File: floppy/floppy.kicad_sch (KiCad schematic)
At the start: 4 parts, among them J1 driveint, J2 perslota, J3 perslotb

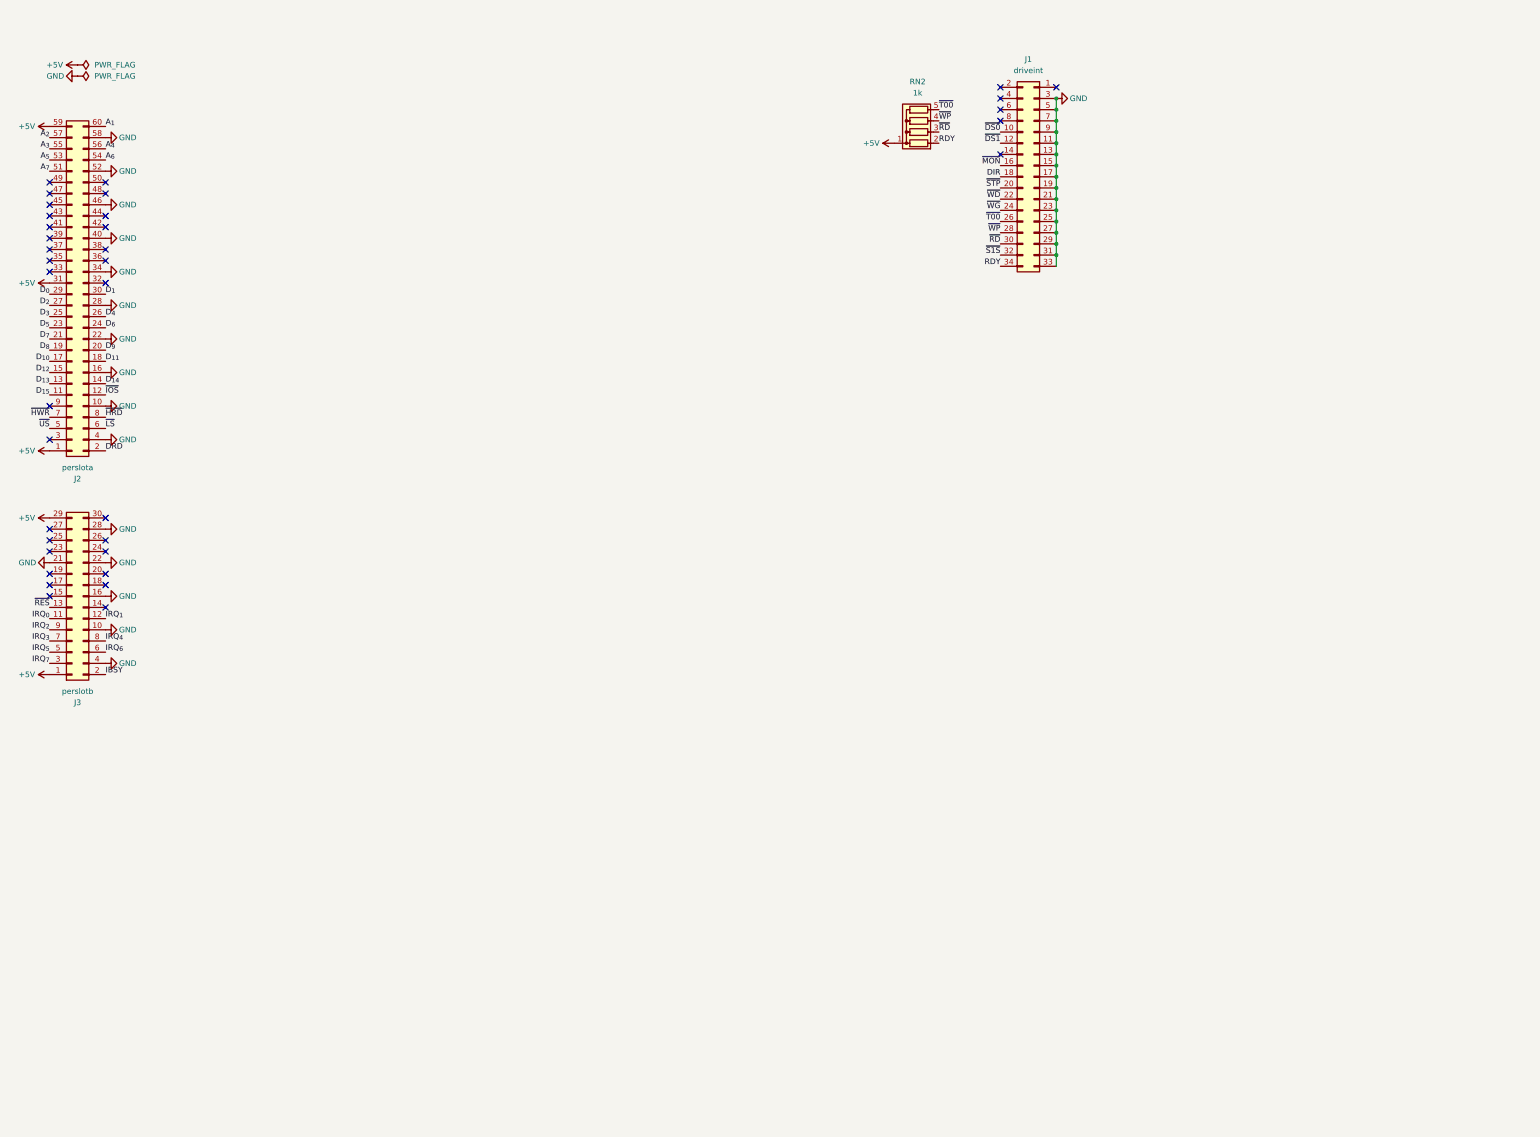
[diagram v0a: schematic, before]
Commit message: [floppy] added the 3.5" HD (custom) floppy controller peripheral
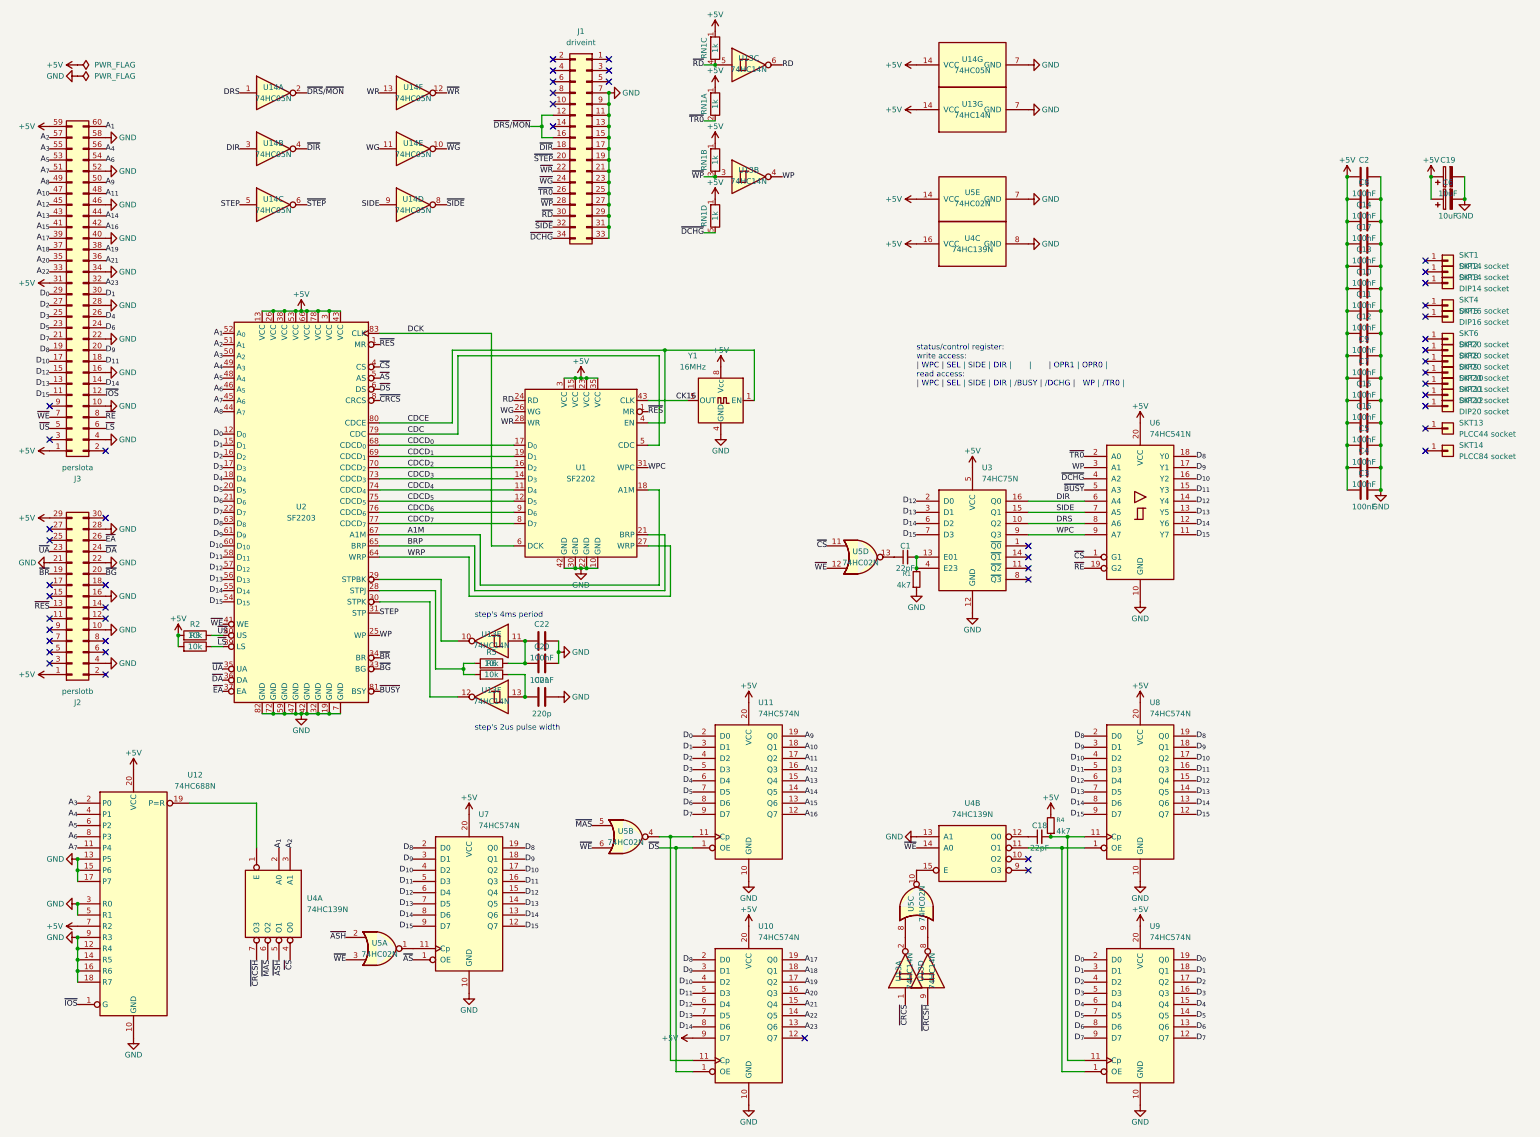
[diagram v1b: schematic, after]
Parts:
- removed RN2: 1k, Resistor_THT:R_Array_SIP5, symbol Device:R_Network04
- added C1, C18: 22pF, Capacitor_THT:C_Disc_D3.0mm_W1.6mm_P2.54mm, symbol Device:C_Small
- added C10, C11, C12, C13, C14, C17, C2, C20, C22, C7, C8, C9: 100nF, Capacitor_THT:C_Disc_D3.0mm_W1.6mm_P2.54mm, symbol Device:C
- added C15, C16, C3, C4, C5: 100nF, Capacitor_THT:C_Disc_D3.0mm_W1.6mm_P7.62mm, symbol Device:C
- added C19, C6: 10uF, Capacitor_THT:CP_Radial_D5.0mm_P2.00mm, symbol Device:C_Polarized
- added C21: 220p, Capacitor_THT:C_Disc_D3.0mm_W1.6mm_P2.54mm, symbol Device:C
- added R1, R4: 4k7, Resistor_THT:R_Axial_DIN0207_L6.3mm_D2.5mm_P2.54mm_Vertical, symbol Device:R_Small
- added R2, R3, R5, R6: 10k, Resistor_THT:R_Axial_DIN0207_L6.3mm_D2.5mm_P2.54mm_Vertical, symbol Device:R
- added RN1: 1k, Resistor_THT:R_Array_SIP5, symbol Device:R_Network04_Split
- added SKT1, SKT2, SKT3: DIP14 socket, symbol Connector_Generic:Conn_01x01
- added SKT10, SKT11, SKT12, SKT6, SKT7, SKT8, SKT9: DIP20 socket, symbol Connector_Generic:Conn_01x01
- added SKT13: PLCC44 socket, symbol Connector_Generic:Conn_01x01
- added SKT14: PLCC84 socket, symbol Connector_Generic:Conn_01x01
- added SKT4, SKT5: DIP16 socket, symbol Connector_Generic:Conn_01x01
- added U1: SF2202, Package_LCC:PLCC-44_THT-Socket, symbol SFxxxx:SF2202
- added U10, U11, U7, U8, U9: 74HC574N, Package_DIP:DIP-20_W7.62mm, symbol 74xx:74LS574
- added U12: 74HC688N, Package_DIP:DIP-20_W7.62mm, symbol 74xx:74HC688
- added U13: 74HC14N, Package_DIP:DIP-14_W7.62mm, symbol 74xx:74HC14
- added U14: 74HC05N, Package_DIP:DIP-14_W7.62mm, symbol 74xx:74LS05
- added U2: SF2203, Package_LCC:PLCC-84_THT-Socket, symbol SFxxxx:SF2203
- added U3: 74HC75N, Package_DIP:DIP-16_W7.62mm, symbol 74xx:74LS75
- added U4: 74HC139N, Package_DIP:DIP-16_W7.62mm, symbol 74xx:74LS139
- added U5: 74HC02N, Package_DIP:DIP-14_W7.62mm, symbol 74xx:74HC02
- added U6: 74HC541N, Package_DIP:DIP-20_W7.62mm, symbol 74xx:74LS541
- added Y1: 16MHz, Oscillator:Oscillator_DIP-8, symbol Oscillator:CXO_DIP8
- J1: footprint (none) -> Connector_IDC:IDC-Header_2x17_P2.54mm_Horizontal
- J2: renamed from J3; footprint Connector_IDC:IDC-Header_2x15_P2.54mm_Horizontal -> Connector_PCBEdge:edge_connector_15p_2.54mm; now left out of the parts list
- J3: renamed from J2; footprint Connector_IDC:IDC-Header_2x30_P2.54mm_Horizontal -> Connector_PCBEdge:edge_connector_30p_2.54mm; now left out of the parts list
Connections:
- net ~{MON} is gone; now on net ~{DRS}/~{MON}: J1.16 (Pin_16)
- net +5V: now also C10.1, C11.1, C12.1, C13.1, C14.1, C15.1, C16.1, C17.1, C19.1, C2.1, C3.1, C4.1, C5.1, C6.1, C7.1, C8.1, C9.1, R2.2, R3.2, R4.2, RN1.1 (R1), RN1.1 (R1), RN1.1 (R1), RN1.1 (R1), U1.15 (VCC), U1.23 (VCC), U1.3 (VCC), U1.35 (VCC), U10.20 (VCC), U10.9 (D7), U11.20 (VCC), U12.20 (VCC), U12.7 (R2), U13.14 (VCC), U14.14 (VCC), U2.13 (VCC), U2.26 (VCC), U2.3 (VCC), U2.38 (VCC), U2.43 (VCC), U2.53 (VCC), U2.66 (VCC), U2.78 (VCC), U3.5 (VCC), U4.16 (VCC), U5.14 (VCC), U6.20 (VCC), U7.20 (VCC), U8.20 (VCC), U9.20 (VCC), Y1.8 (Vcc)
- net A_{1}: now also U2.52 (A_{0}), U4.2 (A0)
- net A_{2}: now also U2.51 (A_{1}), U4.3 (A1)
- net A_{3}: now also U12.2 (P0), U2.50 (A_{2})
- net A_{4}: now also U12.4 (P1), U2.49 (A_{3})
- net A_{5}: now also U12.6 (P2), U2.48 (A_{4})
- net A_{6}: now also U12.8 (P3), U2.46 (A_{5})
- net A_{7}: now also U12.11 (P4), U2.45 (A_{6})
- net DIR: now also U14.3, U3.16 (Q0), U6.6 (A4); no longer J1.18 (Pin_18)
- net D_{0}: now also U11.2 (D0), U2.12 (D_{0}), U9.19 (Q0), U9.2 (D0)
- net D_{10}: now also U10.4 (D2), U2.60 (D_{10}), U6.16 (Y2), U7.17 (Q2), U7.4 (D2), U8.17 (Q2), U8.4 (D2)
- net D_{11}: now also U10.5 (D3), U2.58 (D_{11}), U6.15 (Y3), U7.16 (Q3), U7.5 (D3), U8.16 (Q3), U8.5 (D3)
- net D_{12}: now also U10.6 (D4), U2.57 (D_{12}), U3.2 (D0), U6.14 (Y4), U7.15 (Q4), U7.6 (D4), U8.15 (Q4), U8.6 (D4)
- net D_{13}: now also U10.7 (D5), U2.56 (D_{13}), U3.3 (D1), U6.13 (Y5), U7.14 (Q5), U7.7 (D5), U8.14 (Q5), U8.7 (D5)
- net D_{14}: now also U10.8 (D6), U2.55 (D_{14}), U3.6 (D2), U6.12 (Y6), U7.13 (Q6), U7.8 (D6), U8.13 (Q6), U8.8 (D6)
- net D_{15}: now also U2.54 (D_{15}), U3.7 (D3), U6.11 (Y7), U7.12 (Q7), U7.9 (D7), U8.12 (Q7), U8.9 (D7)
- net D_{1}: now also U11.3 (D1), U2.15 (D_{1}), U9.18 (Q1), U9.3 (D1)
- net D_{2}: now also U11.4 (D2), U2.16 (D_{2}), U9.17 (Q2), U9.4 (D2)
- net D_{3}: now also U11.5 (D3), U2.17 (D_{3}), U9.16 (Q3), U9.5 (D3)
- net D_{4}: now also U11.6 (D4), U2.18 (D_{4}), U9.15 (Q4), U9.6 (D4)
- net D_{5}: now also U11.7 (D5), U2.20 (D_{5}), U9.14 (Q5), U9.7 (D5)
- net D_{6}: now also U11.8 (D6), U2.21 (D_{6}), U9.13 (Q6), U9.8 (D6)
- net D_{7}: now also U11.9 (D7), U2.22 (D_{7}), U9.12 (Q7), U9.9 (D7)
- net D_{8}: now also U10.2 (D0), U2.63 (D_{8}), U6.18 (Y0), U7.19 (Q0), U7.2 (D0), U8.19 (Q0), U8.2 (D0)
- net D_{9}: now also U10.3 (D1), U2.61 (D_{9}), U6.17 (Y1), U7.18 (Q1), U7.3 (D1), U8.18 (Q1), U8.3 (D1)
- net GND: now also C10.2, C11.2, C12.2, C13.2, C14.2, C15.2, C16.2, C17.2, C19.2, C2.2, C20.2, C21.2, C22.2, C3.2, C4.2, C5.2, C6.2, C7.2, C8.2, C9.2, R1.1, U1.10 (GND), U1.22 (GND), U1.30 (GND), U1.42 (GND), U10.10 (GND), U11.10 (GND), U12.10 (GND), U12.12 (R4), U12.13 (P5), U12.14 (R5), U12.15 (P6), U12.16 (R6), U12.17 (P7), U12.18 (R7), U12.3 (R0), U12.5 (R1), U12.9 (R3), U13.7 (GND), U14.7 (GND), U2.19 (GND), U2.32 (GND), U2.42 (GND), U2.47 (GND), U2.59 (GND), U2.7 (GND), U2.72 (GND), U2.82 (GND), U3.12 (GND), U4.13 (A1), U4.8 (GND), U5.7 (GND), U6.10 (GND), U7.10 (GND), U8.10 (GND), U9.10 (GND), Y1.4 (GND); no longer J1.3 (Pin_3), J1.5 (Pin_5)
- net ~{IOS}: now also U12.1 (G)
- net ~{LS}: now also R3.1, U2.39 (LS)
- net ~{RD}: now also RN1.4 (R3.2), U13.5
- net ~{RES}: now also U1.1 (MR), U2.1 (MR)
- net ~{US}: now also R2.1, U2.40 (US)
- net ~{WG}: now also U14.10
- net ~{WP}: now also RN1.3 (R2.2), U13.3
- net ~{BR}: now reaches J2.19 (Pin_19)
- net ~{BR}: now also U2.34 (BR)
- net ~{BG}: now reaches J2.20 (Pin_20)
- net ~{BG}: now also U2.33 (BG)
- net ~{UA}: now reaches J2.23 (Pin_23)
- net ~{UA}: now also U2.35 (UA)
- net ~{DA}: now reaches J2.24 (Pin_24)
- net ~{DA}: now also U2.36 (DA)
- net ~{EA}: now reaches J2.26 (Pin_26)
- net ~{EA}: now also U2.37 (EA)
- net A_{23}: now reaches J3.32 (Pin_32)
- net A_{23}: now also U10.13 (Q6)
- net A_{22}: now reaches J3.33 (Pin_33)
- net A_{22}: now also U10.14 (Q5)
- net A_{20}: now reaches J3.35 (Pin_35)
- net A_{20}: now also U10.16 (Q3)
- net A_{21}: now reaches J3.36 (Pin_36)
- net A_{21}: now also U10.15 (Q4)
- net A_{18}: now reaches J3.37 (Pin_37)
- net A_{18}: now also U10.18 (Q1)
- net A_{19}: now reaches J3.38 (Pin_38)
- net A_{19}: now also U10.17 (Q2)
- net A_{17}: now reaches J3.39 (Pin_39)
- net A_{17}: now also U10.19 (Q0)
- net A_{15}: now reaches J3.41 (Pin_41)
- net A_{15}: now also U11.13 (Q6)
- net A_{16}: now reaches J3.42 (Pin_42)
- net A_{16}: now also U11.12 (Q7)
- net A_{13}: now reaches J3.43 (Pin_43)
- net A_{13}: now also U11.15 (Q4)
- net A_{14}: now reaches J3.44 (Pin_44)
- net A_{14}: now also U11.14 (Q5)
- net A_{12}: now reaches J3.45 (Pin_45)
- net A_{12}: now also U11.16 (Q3)
- net A_{10}: now reaches J3.47 (Pin_47)
- net A_{10}: now also U11.18 (Q1)
- net A_{11}: now reaches J3.48 (Pin_48)
- net A_{11}: now also U11.17 (Q2)
- net A_{8}: now reaches J3.49 (Pin_49)
- net A_{8}: now also U2.44 (A_{7})
- net A_{9}: now reaches J3.50 (Pin_50)
- net A_{9}: now also U11.19 (Q0)
- net DRD: no longer names the net of J3.2 (Pin_2)
- net IBSY: no longer names the net of J2.2 (Pin_2)
- net IRQ_{0}: no longer names the net of J2.11 (Pin_11)
- net IRQ_{1}: no longer names the net of J2.12 (Pin_12)
- net IRQ_{2}: no longer names the net of J2.9 (Pin_9)
- net IRQ_{3}: no longer names the net of J2.7 (Pin_7)
- net IRQ_{4}: no longer names the net of J2.8 (Pin_8)
- net IRQ_{5}: no longer names the net of J2.5 (Pin_5)
- net IRQ_{6}: no longer names the net of J2.6 (Pin_6)
- net IRQ_{7}: no longer names the net of J2.3 (Pin_3)
- net RDY renamed ~{DCHG}
- net ~{DCHG}: now also RN1.5 (R4.2), U6.4 (A2)
- net ~{DS0}: no longer names the net of J1.10 (Pin_10)
- net ~{DS1} renamed ~{DRS}/~{MON}
- net ~{DRS}/~{MON}: now also U14.2
- net ~{HRD} renamed ~{RE}
- net ~{RE}: now also U6.19 (G2)
- net ~{HWR} renamed ~{WE}
- net ~{WE}: now also U2.41 (WE), U4.14 (A0), U5.12, U5.3, U5.6
- net ~{S1S} renamed ~{SIDE}
- net ~{SIDE}: now also U14.8
- net ~{STP} renamed ~{STEP}
- net ~{STEP}: now also U14.6
- net ~{T00} renamed ~{TR0}
- net ~{TR0}: now also RN1.2 (R1.2), U6.2 (A0)
- net ~{WD} renamed ~{WR}
- net ~{WR}: now also U14.12
- new net: R5.2, R6.2, U2.28 (STPJ)
- new net: U13.10, U2.29 (STPBK)
- new net: U13.12, U2.30 (STPK)
- new net: C18.1, U4.12 (O0)
- new net: C18.2, R4.1, U8.11 (Cp), U9.11 (Cp)
- new net: C20.1, C22.1, R5.1, U13.11
- new net: C21.1, R6.1, U13.13
- new net: U4.15 (E), U5.10
- new net: U13.2, U5.8
- new net: U13.8, U5.9
- new net: U5.1, U7.11 (Cp)
- new net: C1.1, U5.13
- new net: C1.2, R1.2, U3.13 (E01), U3.4 (E23)
- new net: U12.19 (P=R), U4.1 (E)
- new net: U10.11 (Cp), U11.11 (Cp), U5.4
- new net: U4.11 (O1), U8.1 (OE), U9.1 (OE)
- new net A1M: U1.18 (A1M), U2.67 (A1M)
- new net BRP: U1.21 (BRP), U2.65 (BRP)
- new net CDC: U1.5 (CDC), U2.79 (CDC)
- new net CDCD_{0}: U1.17 (D_{0}), U2.68 (CDCD_{0})
- new net CDCD_{1}: U1.19 (D_{1}), U2.69 (CDCD_{1})
- new net CDCD_{2}: U1.16 (D_{2}), U2.70 (CDCD_{2})
- new net CDCD_{3}: U1.14 (D_{3}), U2.73 (CDCD_{3})
- new net CDCD_{4}: U1.11 (D_{4}), U2.74 (CDCD_{4})
- new net CDCD_{5}: U1.12 (D_{5}), U2.75 (CDCD_{5})
- new net CDCD_{6}: U1.9 (D_{6}), U2.76 (CDCD_{6})
- new net CDCD_{7}: U1.8 (D_{7}), U2.77 (CDCD_{7})
- new net CDCE: U1.4 (EN), U2.80 (CDCE), Y1.1 (EN)
- new net CK16: U1.43 (CLK), Y1.5 (OUT)
- new net DCK: U1.6 (DCK), U2.83 (CLK)
- new net DRS: U14.1, U3.10 (Q2), U6.8 (A6)
- new net RD: U1.24 (RD), U13.6
- new net SIDE: U14.9, U3.15 (Q1), U6.7 (A5)
- new net STEP: U14.5, U2.31 (STP)
- new net WG: U1.26 (WG), U14.11
- new net WP: U13.4, U2.25 (WP), U6.3 (A1)
- new net WPC: U1.31 (WPC), U3.9 (Q3), U6.9 (A7)
- new net WR: U1.28 (WR), U14.13
- new net WRP: U1.27 (WRP), U2.64 (WRP)
- new net ~{ASH}: U4.5 (O1), U5.2
- new net ~{AS}: U2.5 (AS), U7.1 (OE)
- new net ~{BUSY}: U2.81 (BSY), U6.5 (A3)
- new net ~{CRCSH}: U13.9, U4.7 (O3)
- new net ~{CRCS}: U13.1, U2.8 (CRCS)
- new net ~{CS}: U2.4 (CS), U4.4 (O0), U5.11, U6.1 (G1)
- new net ~{DIR}: J1.18 (Pin_18), U14.4
- new net ~{DS}: U10.1 (OE), U11.1 (OE), U2.6 (DS)
- new net ~{MAS}: U4.6 (O2), U5.5
- no-connect marks 36 -> 49
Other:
- note added: "status/control register: write access: | WPC | SEL | SIDE | DIR | | | OPR1 | OPR0 | read access: | WPC | SEL | SIDE | DIR | /BUSY | /DCHG | WP | /TR0 |"
- note added: "step's 2us pulse width"
- note added: "step's 4ms period"
- moved on the sheet: J1
